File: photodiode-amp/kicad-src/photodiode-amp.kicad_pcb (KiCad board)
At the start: 2 copper layers, 24.9 x 26.7 mm, 10 parts, among them J2 Conn_01x04, U1 OPA333xxDBV

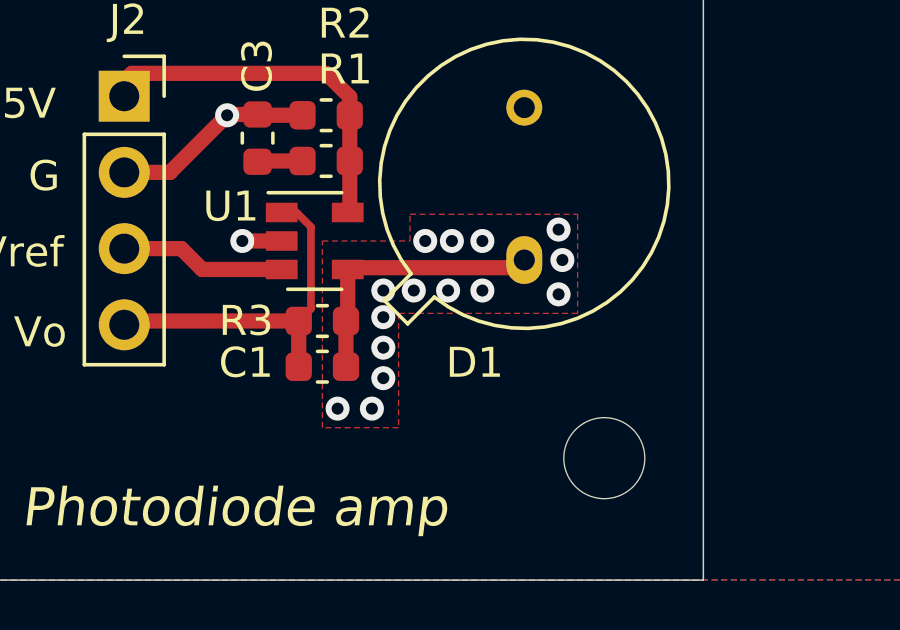
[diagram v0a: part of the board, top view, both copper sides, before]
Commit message: creates pd amp prod files
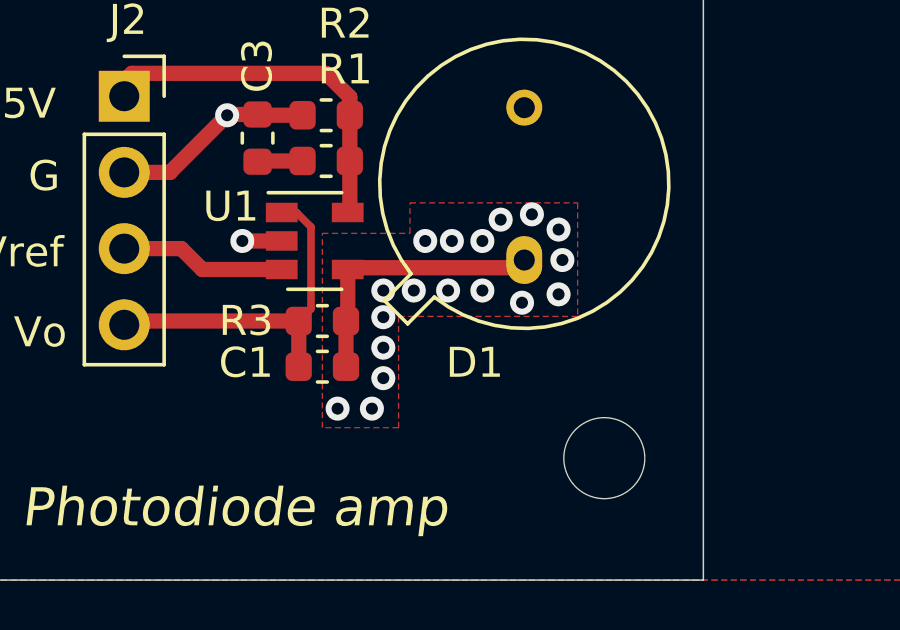
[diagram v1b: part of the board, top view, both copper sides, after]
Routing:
- net GND: vias 17 -> 20
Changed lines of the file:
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@@
     (thickness 1.6)
     (drawings 11)
-    (tracks 50)
+    (tracks 53)
     (zones 0)
     (modules 10)
@@
     (effects (font (size 1.27 1.27) (thickness 0.2286) italic))
   )
-  (gr_text "12/7/2021\n" (at 157.099 85.725) (layer F.Mask)
+  (gr_text "12/7/2021\n" (at 159.385 88.9) (layer F.Mask)
     (effects (font (size 1 1) (thickness 0.15) italic))
   )
@@
   (via (at 160.147 99.822) (size 0.8) (drill 0.4) (layers F.Cu B.Cu) (net 1))
   (via (at 160.02 98.806) (size 0.8) (drill 0.4) (layers F.Cu B.Cu) (net 1))
+  (via (at 158.8008 101.2444) (size 0.8) (drill 0.4) (layers F.Cu B.Cu) (net 1))
+  (via (at 159.131 98.298) (size 0.8) (drill 0.4) (layers F.Cu B.Cu) (net 1))
+  (via (at 158.0896 98.4758) (size 0.8) (drill 0.4) (layers F.Cu B.Cu) (net 1))
   (segment (start 150.0125 96.52) (end 149.987 96.5455) (width 0.508) (layer F.Cu) (net 2))
   (segment (start 151.4855 96.52) (end 150.0125 96.52) (width 0.508) (layer F.Cu) (net 2))
@@
     (polygon
       (pts
-        (xy 160.655 101.6) (xy 154.686 101.6) (xy 154.686 105.41) (xy 152.146 105.41) (xy 152.146 99.187)
-        (xy 155.067 99.187) (xy 155.067 98.298) (xy 160.655 98.298)
+        (xy 160.655 101.7016) (xy 154.686 101.7016) (xy 154.686 105.41) (xy 152.146 105.41) (xy 152.146 98.933)
+        (xy 155.067 98.933) (xy 155.067 97.917) (xy 160.655 97.917)
       )
     )

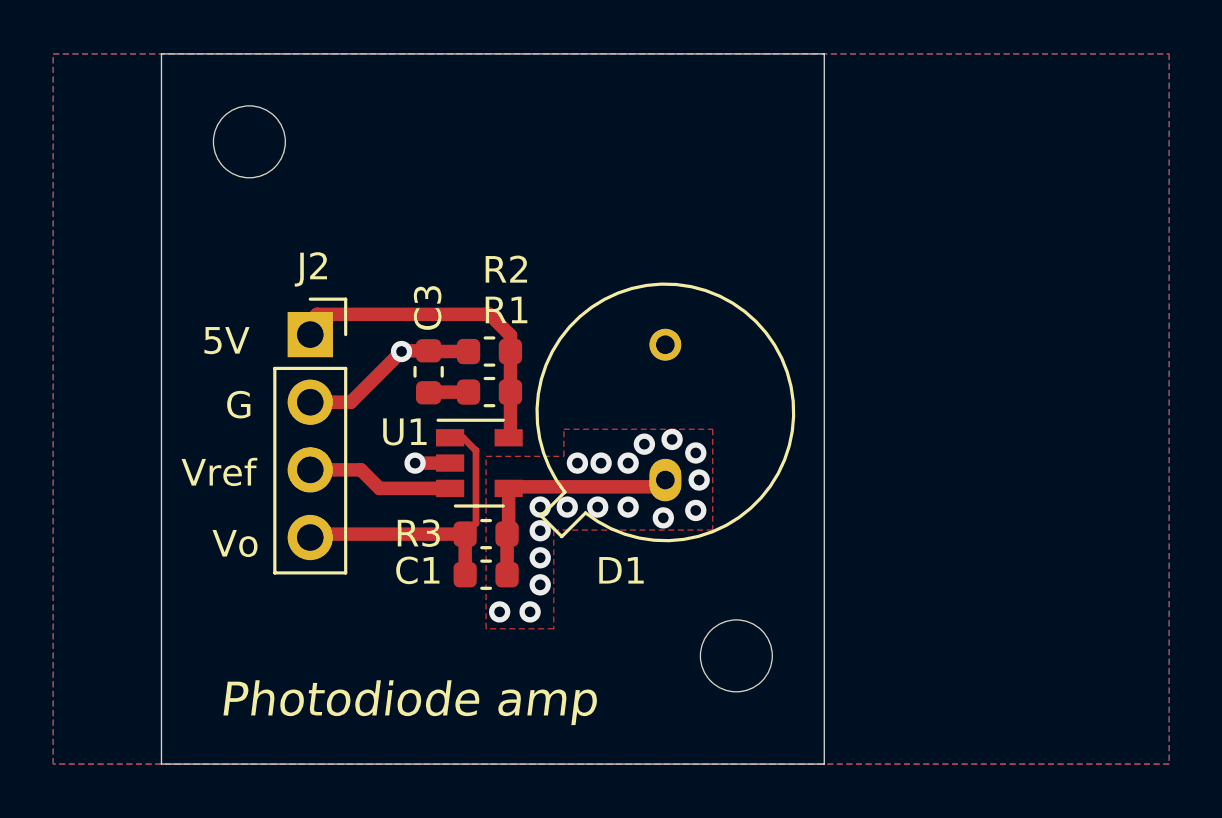
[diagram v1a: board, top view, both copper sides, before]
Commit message: update component values and ids
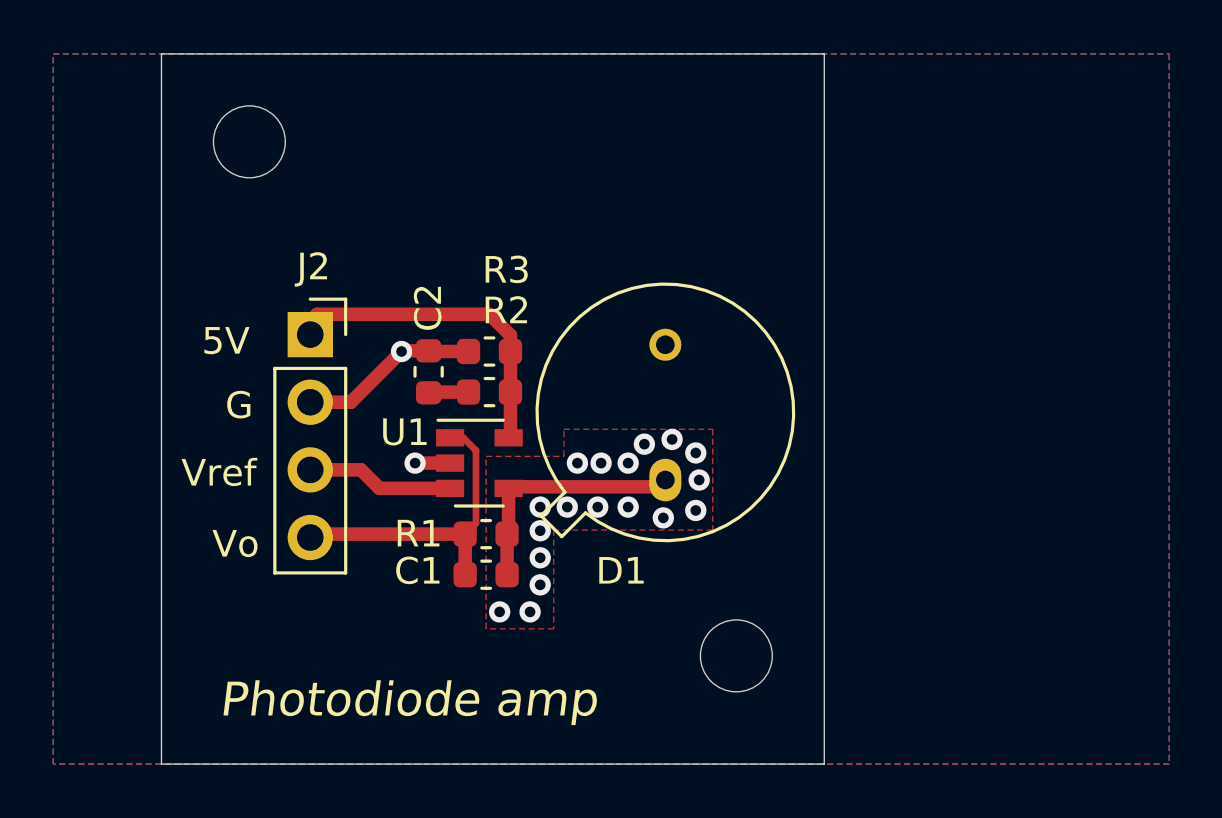
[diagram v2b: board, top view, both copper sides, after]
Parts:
- C2: renamed from C3; value 10nF -> 1uF
- R1: renamed from R3; value 1.2M -> 2M
- R2: renamed from R1; value 100R -> 13.7K
- R3: renamed from R2; value 100R -> 280R
